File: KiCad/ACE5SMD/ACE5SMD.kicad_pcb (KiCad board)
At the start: 2 copper layers, 160 x 100 mm, 100 parts, among them IC1 LM7805_TO220, Q1 MMBT3904, Q3 BC847, X1 CRYSTALHC49U-V 6.556MHz, X2 5MHz

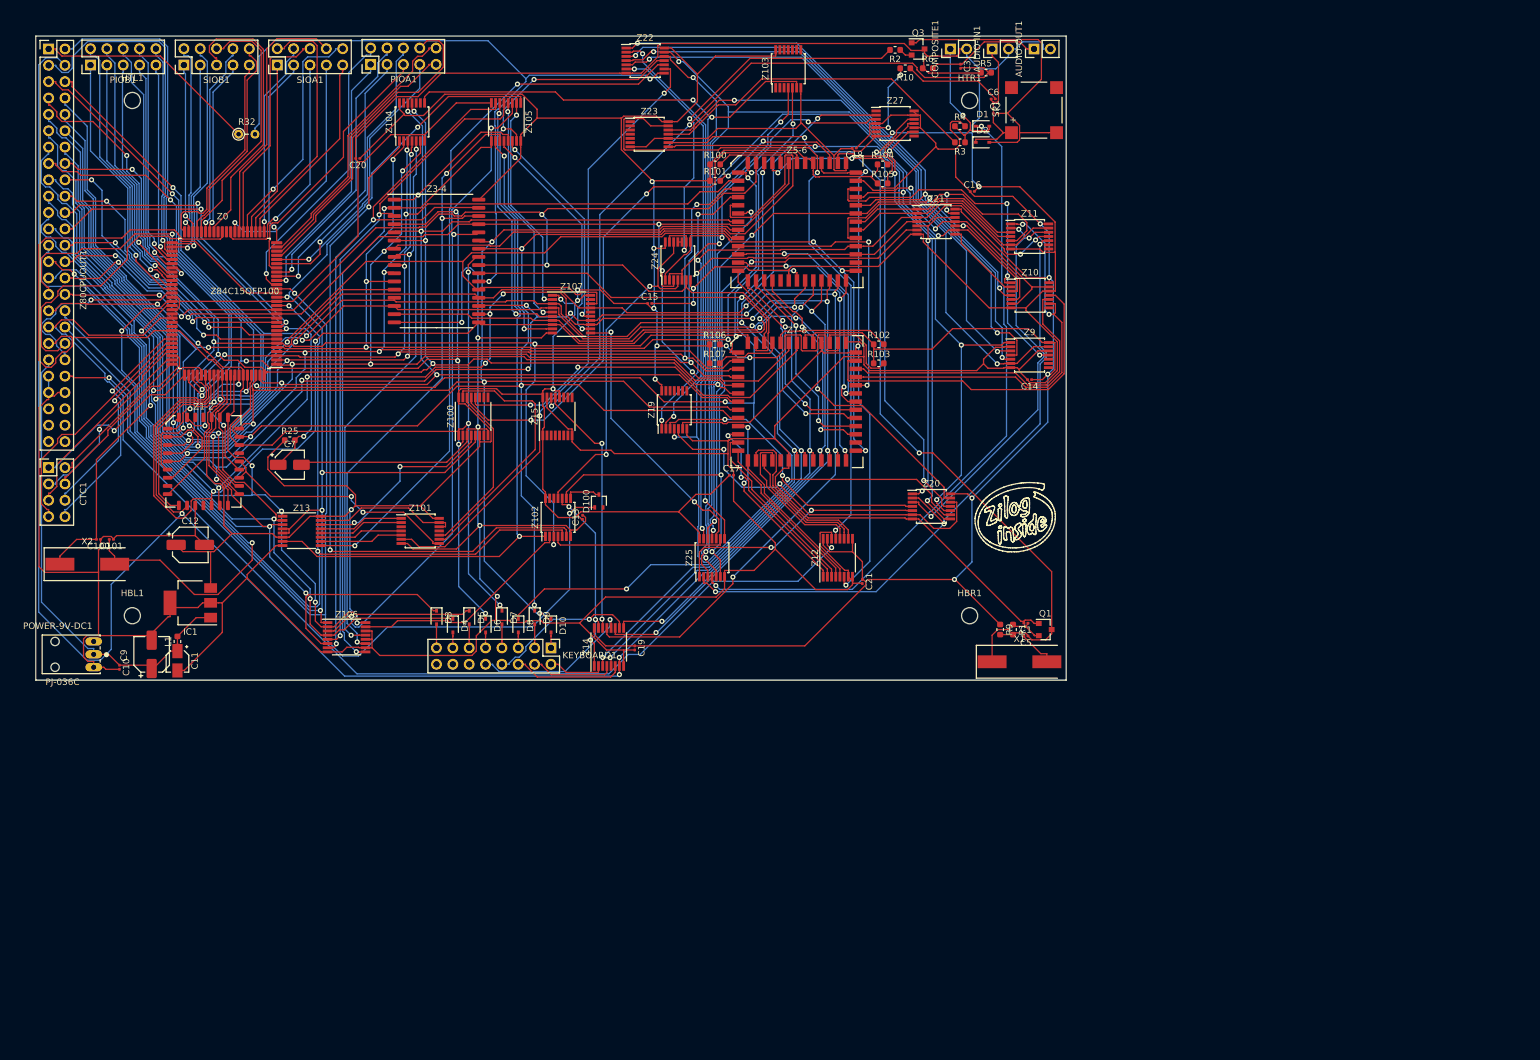
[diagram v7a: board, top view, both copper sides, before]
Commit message: Remove Speakrer leave 2 pin connector add single transistor amp to composite out.
Signed-off-by: John Bradley <flypie@rocketmail.com>
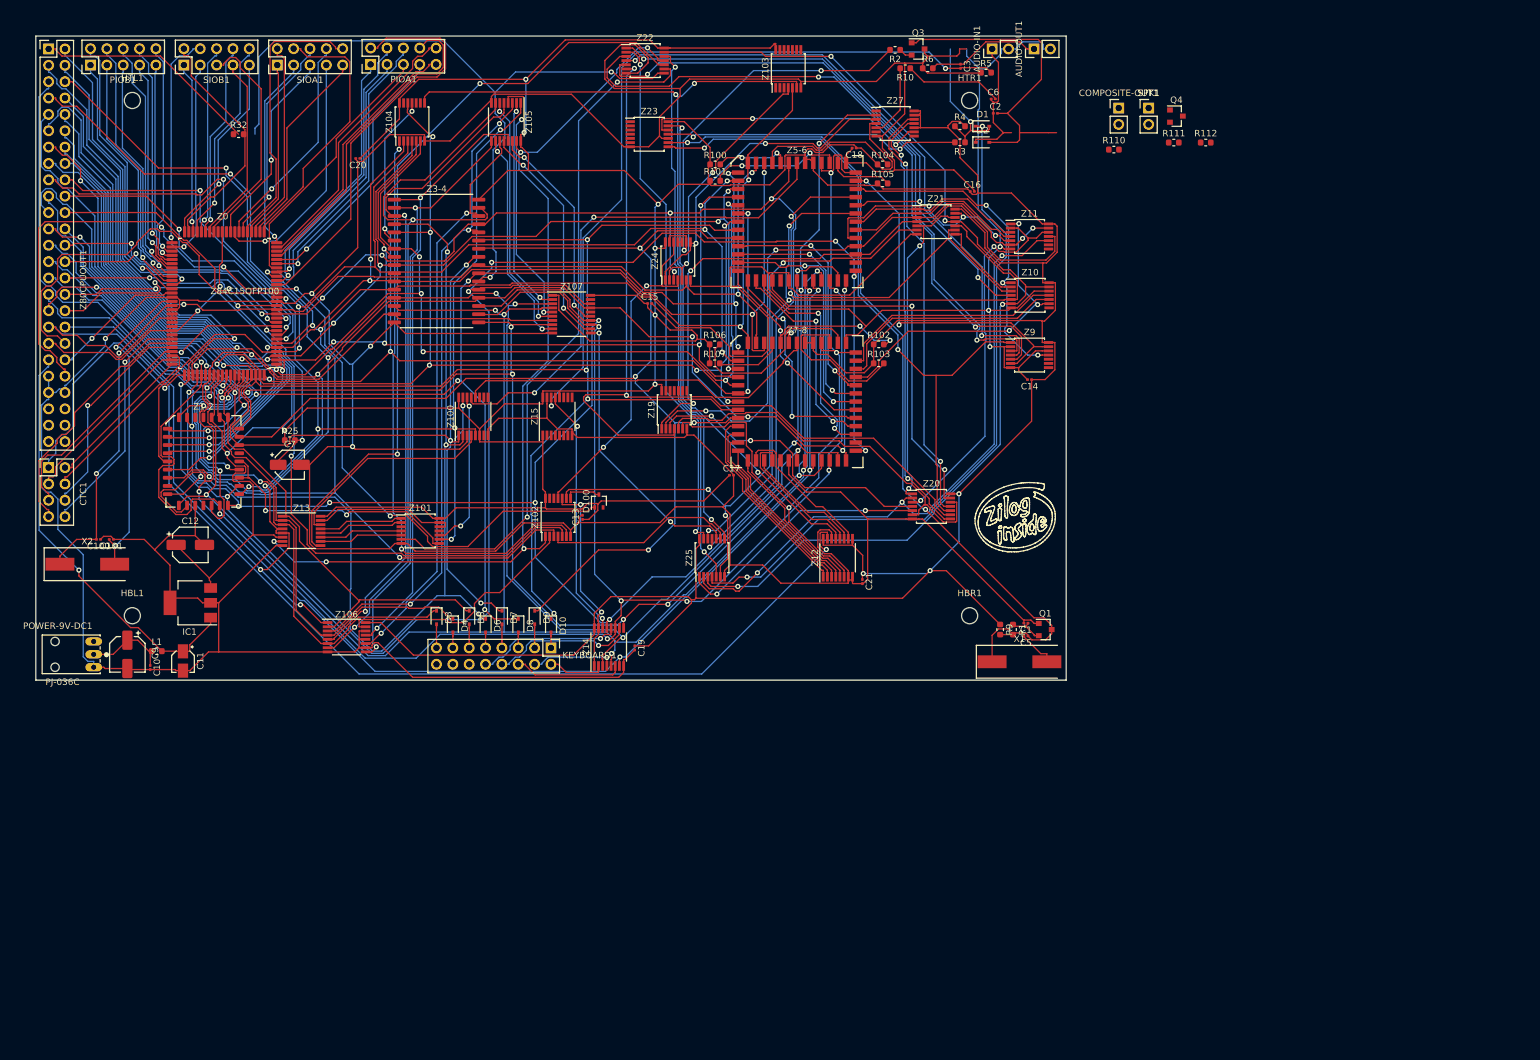
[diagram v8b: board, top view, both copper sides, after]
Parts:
- removed COMPOSITE1: Conn_01x02, Connector_PinHeader_2.54mm:PinHeader_1x02_P2.54mm_Vertical
- removed SP1: Speaker, Buzzer_Beeper:PUIAudio_SMT_0825_S_4_R
- added COMPOSITE-OUT1: COMPOSITE-OUT1, Connector_PinHeader_2.54mm:PinHeader_1x02_P2.54mm_Vertical, F.Cu at (168.1, 11.2)
- added Q4: 2N3904, Package_TO_SOT_SMD:SOT-23, F.Cu at (177.1, 12.4)
- added R110: 200, Resistor_SMD:R_0603_1608Metric, F.Cu at (167.4, 17.6)
- added R111: 100, Resistor_SMD:R_0603_1608Metric, F.Cu at (176.7, 16.5)
- added R112: 18, Resistor_SMD:R_0603_1608Metric, F.Cu at (181.7, 16.5)
- added SPK1: SPK1, Connector_PinHeader_2.54mm:PinHeader_1x02_P2.54mm_Vertical, F.Cu at (172.8, 11.2)
- R32: footprint Resistor_THT:R_Axial_DIN0204_L3.6mm_D1.6mm_P2.54mm_Vertical -> Resistor_SMD:R_0603_1608Metric
- moved C10 4.78 mm to (17.8, 98.0)
- moved C9 3.78 mm to (14.2, 96.0), turned to 270 degrees
- moved L1 3.54 mm to (18.8, 95.5), turned to 0 degrees
- moved C11 0.86 mm to (22.9, 97.0)
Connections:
- C11 pad 1: +9V -> +9Vsm
- IC1 pad 1: +9V -> +9Vsm
- L1 pad 2: +9V -> +9Vsm
- Z80CPUOUT1 pad 39: +9V -> +9Vsm
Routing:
- net +5V: track 849.7 -> 935.0 mm, vias 16 -> 13
- net /DA2: track 384.2 -> 314.6 mm, vias 6 -> 5
- net +9Vsm: track 0.00 -> 65.4 mm, vias 0 -> 1
- net /A10: track 316.4 -> 252.4 mm
- net /A5: track 289.1 -> 226.3 mm, vias 5 -> 7
- net +9V: track 73.9 -> 12.8 mm
- net /DA0: track 295.1 -> 343.2 mm, vias 8 -> 10
- net /DA7: track 274.9 -> 321.3 mm, vias 6 -> 8
- net //RD: track 187.3 -> 143.6 mm
- net /DA1: track 280.3 -> 318.5 mm
- net Net-(C101-Pad2): track 84.0 -> 48.8 mm
- net /DA4: track 261.8 -> 295.8 mm, vias 10 -> 9
- net //IOREQ: track 154.6 -> 124.5 mm, vias 2 -> 3
- net //INT: track 177.3 -> 148.7 mm, vias 3 -> 4
- net Net-(Z12-Pad13): track 106.4 -> 78.2 mm
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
